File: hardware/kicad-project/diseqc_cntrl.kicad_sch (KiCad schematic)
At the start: 28 parts, among them IC1 TPS560200DBVR, J1 Barrel Jack

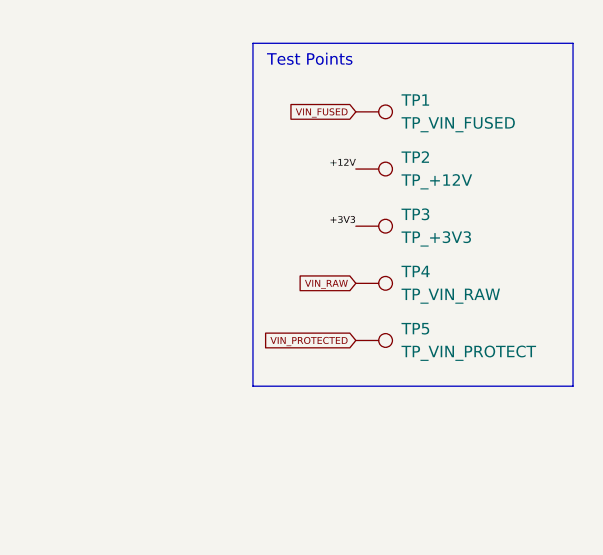
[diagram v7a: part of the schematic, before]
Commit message: Placed LNBH26
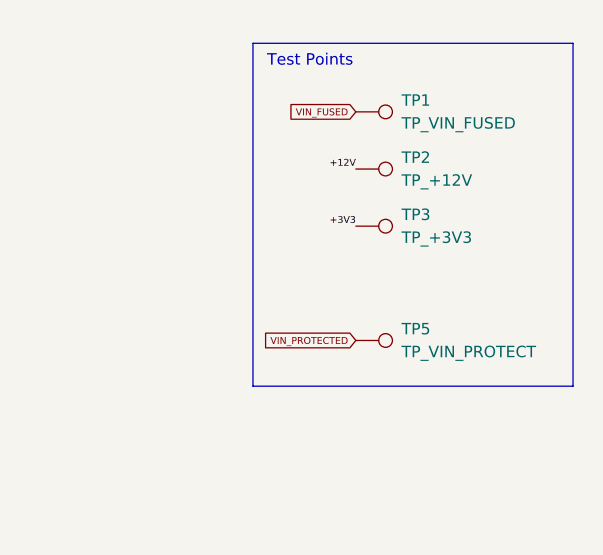
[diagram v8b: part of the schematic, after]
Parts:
- removed TP4: TP_VIN_RAW, TestPoint:TestPoint_THTPad_D1.0mm_Drill0.5mm, symbol Connector:TestPoint
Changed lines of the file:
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@@
 		)
 	)
-	(global_label "VIN_RAW"
-		(shape input)
-		(at 245.11 118.11 180)
-		(fields_autoplaced yes)
-		(effects
-			(font
-				(size 0.762 0.762)
-			)
-			(justify right)
-		)
-		(property "Intersheetrefs" "${INTERSHEET_REFS}"
-			(at 239.0302 118.11 0)
-			(hide yes)
-			(show_name no)
-			(do_not_autoplace no)
-			(effects
-				(font
-					(size 1.27 1.27)
-				)
-				(justify right)
-			)
-		)
-	)
 	(symbol
 		(lib_id "#InvenTree:R_61k9_0603_1%")
@@
 					(unit 1)
 				)
-			)
-		)
-	)
-	(symbol
-		(lib_id "Connector:TestPoint")
-		(at 245.11 118.11 270)
-		(unit 1)
-		(body_style 1)
-		(exclude_from_sim no)
-		(in_bom no)
-		(on_board yes)
-		(in_pos_files yes)
-		(dnp no)
-		(fields_autoplaced yes)
-		(property "Reference" "TP4"
-			(at 250.19 116.8399 90)
-			(show_name no)
-			(do_not_autoplace no)
-			(effects
-				(font
-					(size 1.27 1.27)
-				)
-				(justify left)
-			)
-		)
-		(property "Value" "TP_VIN_RAW"
-			(at 250.19 119.3799 90)
-			(show_name no)
-			(do_not_autoplace no)
-			(effects
-				(font
-					(size 1.27 1.27)
-				)
-				(justify left)
-			)
-		)
-		(property "Footprint" "TestPoint:TestPoint_THTPad_D1.0mm_Drill0.5mm"
-			(at 245.11 123.19 0)
-			(hide yes)
-			(show_name no)
-			(do_not_autoplace no)
-			(effects
-				(font
-					(size 1.27 1.27)
-				)
-			)
-		)
-		(property "Datasheet" ""
-			(at 245.11 123.19 0)
-			(hide yes)
-			(show_name no)
-			(do_not_autoplace no)
-			(effects
-				(font
-					(size 1.27 1.27)
-				)
-			)
-		)
-		(property "Description" "test point"
-			(at 245.11 118.11 0)
-			(hide yes)
-			(show_name no)
-			(do_not_autoplace no)
-			(effects
-				(font
-					(size 1.27 1.27)
-				)
-			)
-		)
-		(property "InvenTree Part" ""
-			(at 245.11 118.11 90)
-			(hide yes)
-			(show_name no)
-			(do_not_autoplace no)
-			(effects
-				(font
-					(size 1.27 1.27)
-				)
-			)
-		)
-		(property "KLC_S4.2_3V3OUT" ""
-			(at 245.11 118.11 90)
-			(hide yes)
-			(show_name no)
-			(do_not_autoplace no)
-			(effects
-				(font
-					(size 1.27 1.27)
-				)
-			)
-		)
-		(property "KLC_S4.2_VCC" ""
-			(at 245.11 118.11 90)
-			(hide yes)
-			(show_name no)
-			(do_not_autoplace no)
-			(effects
-				(font
-					(size 1.27 1.27)
-				)
-			)
-		)
-		(property "Tolerance" ""
-			(at 245.11 118.11 90)
-			(hide yes)
-			(show_name no)
-			(do_not_autoplace no)
-			(effects
-				(font
-					(size 1.27 1.27)
-				)
-			)
-		)
-		(pin "1"
-		)
-		(instances
-			(project "diseqc_cntrl"
-				(path "/82a905d8-f1d7-4995-9c16-94cf3cdcaad9"
-					(reference "TP4")
-					(unit 1)
-				)
